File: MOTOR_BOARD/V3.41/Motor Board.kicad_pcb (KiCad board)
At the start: 2 copper layers, 90.9 x 130.4 mm, 173 parts, among them J1 RJ12, K10 CONN_2, K2 CONN_4, K3 CONN_4, K4 CONN_3, K5 CONN_3, K8 COLONETTE, K9 COLONETTE, P1 CAVALIER, P10 CAVALIER, P11 CONN_4, P2 CONN_4, P3 CAVALIER, P4 CONN_6, P5 CONN_4, P6 CONN_5, P7 CONN_4, P8 CONN_4, P9 CAVALIER, Q1 MOS_N, Q10 2N7002, Q11 2N7002, Q2 MOS_N, Q3 MOS_N, Q4 MOS_N, Q5 MOS_N, Q6 MOS_N, Q7 MOS_N, Q8 MOS_N, Q9 2N7002, SW2 SW_PUSH_SMALL, U1 PCA9306, U10 PIC32MX795F512H, U11 74LVCC3245, U12 74LVCC3245, U13 74LVCC3245, U14 PCA9306, U15 PCF8563, U2 HCTL-2032, U3 74HC02, U4 LM5104, U5 LM5104, U6 74HC02, U7 LM5104, U8 LM5104, U9 24C512, X1 CRYSTAL1

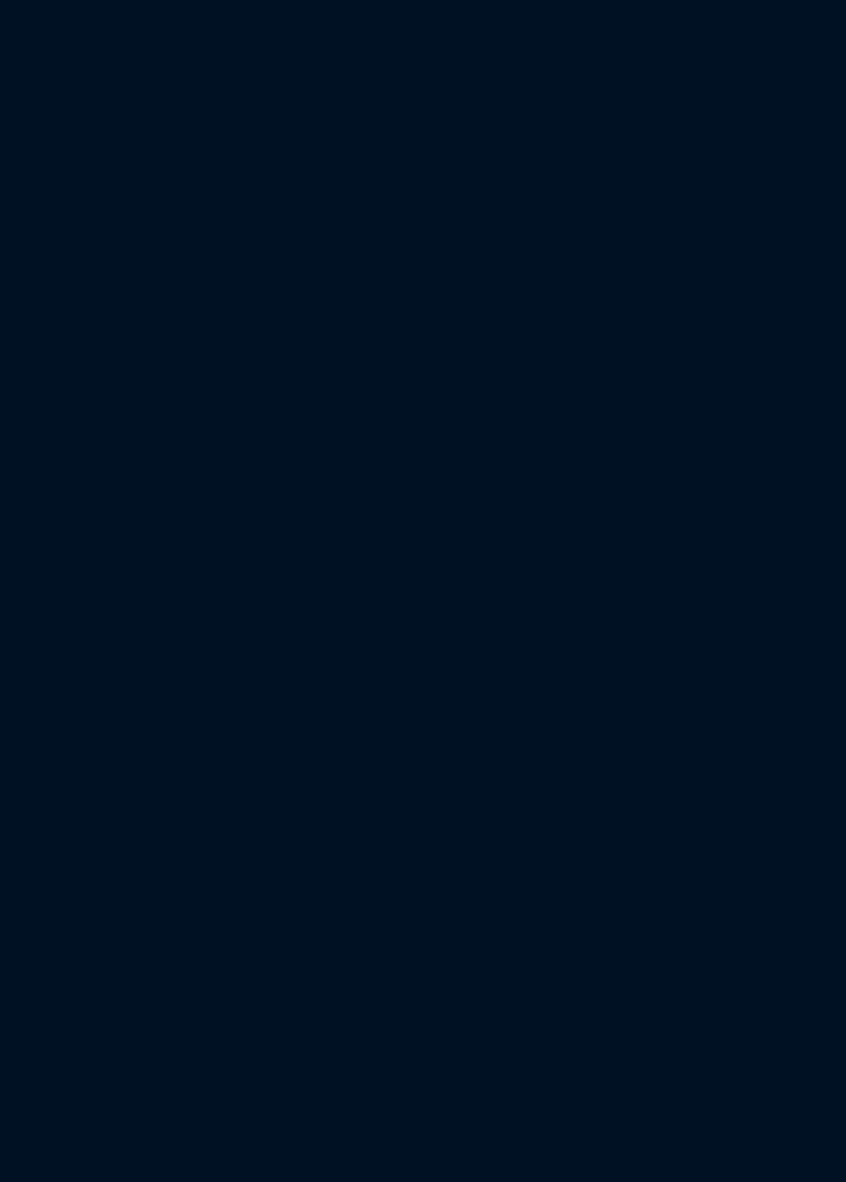
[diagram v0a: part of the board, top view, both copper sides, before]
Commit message: MAJ USB TO 4UART + ADD NEW MECHANICAL BOARD
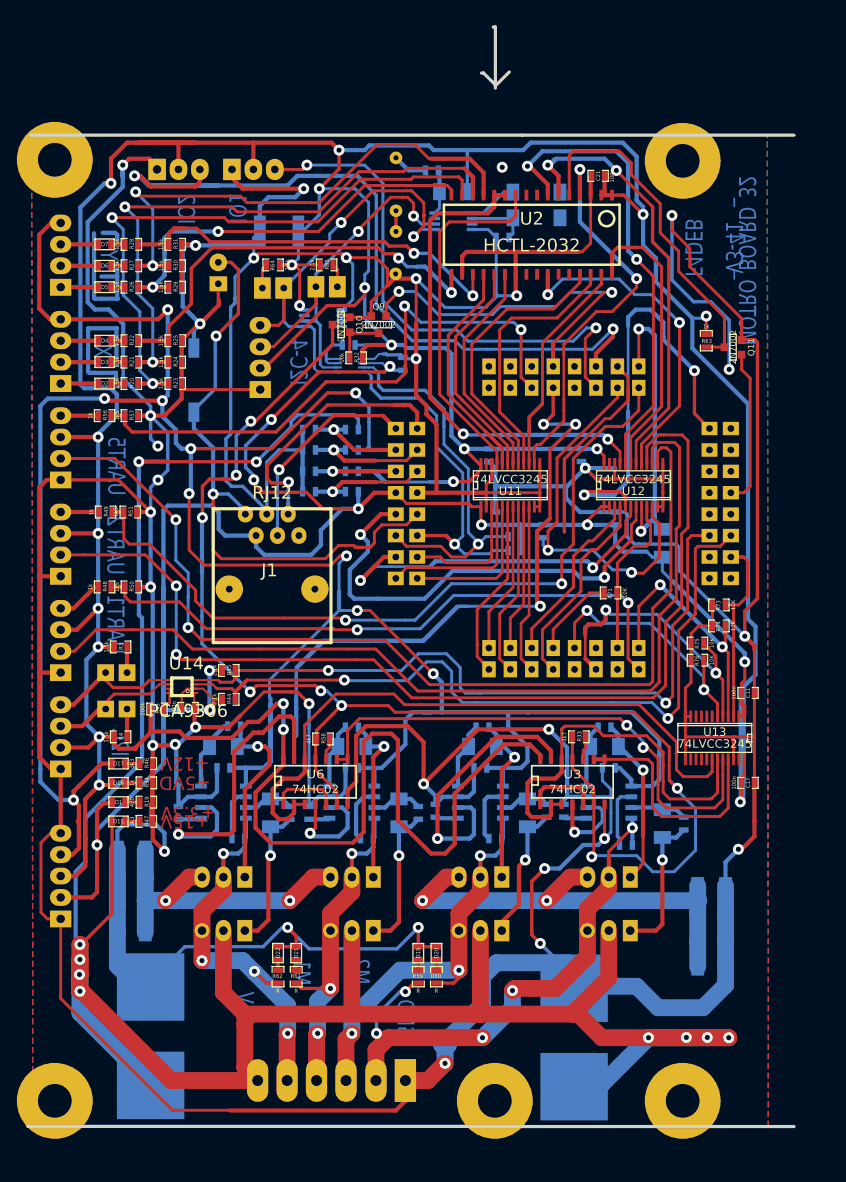
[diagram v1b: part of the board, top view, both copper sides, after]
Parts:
- added 1PIN: P***, 1pin, B.Cu at (50.1, 47.6)
- added C1: 2200u, C_14x16, B.Cu at (61.5, 157.4)
- added C10: 100n, SM0603_Capa, B.Cu at (70.1, 119.8)
- added C11: 100n, SM0603_Capa, F.Cu at (132.3, 110.9)
- added C12: 100n, SM0603_Capa, F.Cu at (65.9, 112.6)
- added C13: 100n, SM0603_Capa, B.Cu at (116.6, 90.2)
- added C14: 100n, SM0603_Capa, B.Cu at (102.4, 90.2)
- added C15: 100n, SM0603_Capa, B.Cu at (101.6, 82.7)
- added C16: 100n, SM0603_Capa, B.Cu at (112.6, 82.7)
- added C17: 100n, SM0603_Capa, F.Cu at (132.3, 121.5)
- added C18: 47u, SM1812, B.Cu at (76.7, 56.1)
- added C19: 2200u, C_14x16, B.Cu at (111.7, 157.6)
- added C2: 100n, SM0603_Capa, B.Cu at (91.4, 71.8)
- added C20: CP, C-10F, B.Cu at (94.4, 44.1)
- added C21: 100n, SM0603_Capa, F.Cu at (114.6, 49.5)
- added C22: CP, C-10F, B.Cu at (94.4, 56.3)
- added C23: C, SM0603_Capa, B.Cu at (103.2, 56.8)
- added C3: 100n, SM0603_Capa, B.Cu at (117.9, 128.9)
- added C4: 100n, SM0603_Capa, B.Cu at (102.4, 128.1)
- added C5: 100n, SM0603_Capa, B.Cu at (115.8, 119.8)
- added C6: 100n, SM0603_Capa, B.Cu at (100.6, 119.8)
- added C7: 100n, SM0603_Capa, B.Cu at (87.1, 128.1)
- added C8: 100n, SM0603_Capa, B.Cu at (71.9, 128.1)
- added C9: 100n, SM0603_Capa, B.Cu at (85.3, 119.8)
- added COLONETTE: VAL**, COLONETTE, B.Cu at (50.1, 47.6)
- added COLONETTE: VAL**, COLONETTE, B.Cu at (102.3, 159.3)
- added COLONETTE: VAL**, COLONETTE, B.Cu at (50.1, 159.3)
- added D1: VERT, SM0603, F.Cu at (57.7, 123.8)
- added D10: DIODE, SM1206, B.Cu at (115.3, 117.2)
- added D11: DIODE, SM1206, B.Cu at (100.8, 117.2)
- added D12: DIODE, SM1206, B.Cu at (90.9, 125.1)
- added D13: DIODE, SM1206, B.Cu at (75.7, 125.1)
- added D14: DIODE, SM1206, B.Cu at (85.3, 117.2)
- added D15: DIODE, SM1206, B.Cu at (70.1, 117.2)
- added D16: VERT, SM0603, F.Cu at (57.7, 121.5)
- added D17: VERT, SM0603, F.Cu at (57.7, 119.3)
- added D18: VERT, SM0603, F.Cu at (57.7, 126.1)
- added D19: LED, SM0603, F.Cu at (93.2, 141.7)
- added D2: JAUNE, SM0603, F.Cu at (56.0, 74.2)
- added D20: LED, SM0603, F.Cu at (95.4, 141.7)
- added D21: LED, SM0603, F.Cu at (78.7, 141.7)
- added D22: LED, SM0603, F.Cu at (76.6, 141.7)
- added D23: DIODESCH, SM1206, B.Cu at (97.4, 51.4)
- added D3: JAUNE, SM0603, F.Cu at (56.0, 71.6)
- added D4: JAUNE, SM0603, F.Cu at (56.0, 69.1)
- added D5: JAUNE, SM0603, F.Cu at (56.0, 62.7)
- added D6: JAUNE, SM0603, F.Cu at (56.0, 60.2)
- added D7: JAUNE, SM0603, F.Cu at (56.0, 57.7)
- added D8: DIODE, SM1206, B.Cu at (122.2, 126.4)
- added D9: DIODE, SM1206, B.Cu at (106.2, 125.1)
- added J1: RJ12, RJ12_E, F.Cu at (75.9, 89.7)
- added K10: CONN_2, KK-2, B.Cu at (69.5, 59.8)
- added K2: CONN_4, KK-4, B.Cu at (50.8, 66.5)
- added K3: CONN_4, KK-4, B.Cu at (50.8, 55.1)
- added K4: CONN_3, KK-3, B.Cu at (67.3, 48.8)
- added K5: CONN_3, KK-3, B.Cu at (76.2, 48.8)
- added K8: COLONETTE, COLONETTE, B.Cu at (124.6, 159.3)
- added K9: COLONETTE, COLONETTE, B.Cu at (124.6, 47.8)
- added P1: CAVALIER, CAVALIER, B.Cu at (56.1, 108.5)
- added P10: CAVALIER, CAVALIER, B.Cu at (81.1, 62.7)
- added P11: CONN_4, KK-4, B.Cu at (74.5, 67.3)
- added P2: CONN_4, KK-4, B.Cu at (50.8, 112.3)
- added P3: CAVALIER, CAVALIER, B.Cu at (56.1, 112.8)
- added P4: CONN_6, WEIDMULLER-6, B.Cu at (91.7, 156.8)
- added P5: CONN_4, KK-4, B.Cu at (50.8, 89.4)
- added P6: CONN_5, KK-5, B.Cu at (50.8, 130.0)
- added P7: CONN_4, KK-4, B.Cu at (50.8, 78.0)
- added P8: CONN_4, KK-4, B.Cu at (50.8, 100.8)
- added P9: CAVALIER, CAVALIER, B.Cu at (77.3, 62.8)
- added Q1: MOS_N, IRFIZ48V, B.Cu at (115.8, 139.1)
- added Q10: 2N7002, SOT23GDS, F.Cu at (84.1, 67.2)
- added Q11: 2N7002, SOT23GDS, F.Cu at (130.6, 69.8)
- added Q2: MOS_N, IRFIZ48V, B.Cu at (100.6, 139.1)
- added Q3: MOS_N, IRFIZ48V, B.Cu at (115.8, 132.7)
- added Q4: MOS_N, IRFIZ48V, B.Cu at (100.6, 132.7)
- added Q5: MOS_N, IRFIZ48V, B.Cu at (85.3, 139.1)
- added Q6: MOS_N, IRFIZ48V, B.Cu at (70.1, 139.1)
- added Q7: MOS_N, IRFIZ48V, B.Cu at (85.3, 132.7)
- added Q8: MOS_N, IRFIZ48V, B.Cu at (70.1, 132.7)
- added Q9: 2N7002, SOT23GDS, F.Cu at (88.5, 67.2)
- added R1: 0.068, SM1206, B.Cu at (128.0, 133.7)
- added R10: 220k, SM0603_Resistor, B.Cu at (95.2, 124.8)
- added R11: 0.068, SM1206, B.Cu at (128.0, 143.4)
- added R12: 47, SM0603_Resistor, B.Cu at (93.2, 125.1)
- added R13: 47, SM0603_Resistor, B.Cu at (78.0, 125.1)
- added R14: 220k, SM0603_Resistor, B.Cu at (80.3, 125.1)
- added R15: 47, SM0603_Resistor, B.Cu at (85.3, 114.9)
- added R16: 47, SM0603_Resistor, B.Cu at (71.4, 114.8)
- added R17: 220k, SM0603_Resistor, B.Cu at (64.8, 125.1)
- added R18: 0.068, SM1206, B.Cu at (59.2, 129.4)
- added R19: 470, SM0603_Resistor, F.Cu at (61.0, 123.8)
- added R2: 0.068, SM1206, B.Cu at (128.0, 140.3)
- added R20: 1.5k, SM0603_Resistor, F.Cu at (59.2, 74.2)
- added R21: 1.5k, SM0603_Resistor, F.Cu at (59.2, 71.6)
- added R22: 1.5k, SM0603_Resistor, F.Cu at (59.2, 69.1)
- added R23: 1.5k, SM0603_Resistor, F.Cu at (64.4, 74.2)
- added R24: 1.5k, SM0603_Resistor, F.Cu at (64.4, 71.6)
- added R25: 1.5k, SM0603_Resistor, F.Cu at (64.4, 69.1)
- added R26: 1.5k, SM0603_Resistor, F.Cu at (59.2, 62.7)
- added R27: 1.5k, SM0603_Resistor, F.Cu at (59.2, 60.2)
- added R28: 1.5k, SM0603_Resistor, F.Cu at (59.2, 57.7)
- added R29: 1.5k, SM0603_Resistor, F.Cu at (64.4, 62.7)
- added R3: 1.5k, SM0603_Resistor, F.Cu at (57.9, 105.4)
- added R30: 1.5k, SM0603_Resistor, F.Cu at (64.4, 60.2)
- added R31: 1.5k, SM0603_Resistor, F.Cu at (64.4, 57.7)
- added R32: 10k, SM0603_Resistor, F.Cu at (85.9, 71.1)
- added R33: 4k7, SM0603_Resistor, F.Cu at (112.3, 116.1)
- added R34: 1k, SM0603_Resistor, F.Cu at (61.0, 121.5)
- added R35: 10k 1%, SM0603_Resistor, B.Cu at (85.3, 79.6)
- added R36: 10k 1%, SM0603_Resistor, B.Cu at (85.3, 82.0)
- added R37: 10k 1%, SM0603_Resistor, B.Cu at (85.3, 84.6)
- added R38: 10k 1%, SM0603_Resistor, B.Cu at (85.3, 87.0)
- added R39: 1k 1%, SM0603_Resistor, B.Cu at (80.3, 79.6)
- added R4: 1.5k, SM0603_Resistor, F.Cu at (57.9, 116.1)
- added R40: 1k 1%, SM0603_Resistor, B.Cu at (80.3, 82.0)
- added R41: 1k 1%, SM0603_Resistor, B.Cu at (80.3, 84.6)
- added R42: 1k 1%, SM0603_Resistor, B.Cu at (80.3, 87.0)
- added R43: 200k, SM0603_Resistor, F.Cu at (62.2, 112.8)
- added R44: 2.1k, SM0603_Resistor, F.Cu at (70.7, 111.6)
- added R45: 2.1k, SM0603_Resistor, F.Cu at (70.7, 108.2)
- added R46: 3k3, SM0603_Resistor, F.Cu at (61.0, 119.3)
- added R47: 3k3, SM0603_Resistor, F.Cu at (61.0, 126.1)
- added R48: 1k, SM0603_Resistor, F.Cu at (56.0, 98.3)
- added R49: 1k, SM0603_Resistor, F.Cu at (56.1, 89.4)
- added R5: 47, SM0603_Resistor, B.Cu at (124.7, 126.4)
- added R50: 1k5, SM0603_Resistor, F.Cu at (59.2, 98.3)
- added R51: 1k5, SM0603_Resistor, F.Cu at (59.1, 89.4)
- added R52: 0.068, SM1206, B.Cu at (128.0, 137.0)
- added R53: 0.068, SM1206, B.Cu at (59.2, 136.0)
- added R54: 0.068, SM1206, B.Cu at (59.2, 139.3)
- added R55: 0.068, SM1206, B.Cu at (59.2, 132.7)
- added R56: 1k, SM0603_Resistor, F.Cu at (56.0, 78.0)
- added R57: 1k5, SM0603_Resistor, F.Cu at (59.2, 78.0)
- added R58: 4k7, SM0603_Resistor, F.Cu at (81.9, 116.3)
- added R59: R, SM0603_Resistor, F.Cu at (93.2, 144.5)
- added R6: 47, SM0603_Resistor, B.Cu at (108.5, 124.8)
- added R60: R, SM0603_Resistor, F.Cu at (95.4, 144.5)
- added R61: R, SM0603_Resistor, F.Cu at (78.7, 144.5)
- added R62: R, SM0603_Resistor, F.Cu at (76.6, 144.5)
- added R63: 1k, SM0603_Resistor, F.Cu at (127.4, 69.1)
- added R64: 2.1k, SM0603_Resistor, F.Cu at (76.0, 60.1)
- added R65: 2.1k, SM0603_Resistor, F.Cu at (82.3, 60.1)
- added R66: 2.1k, SM0603_Resistor, B.Cu at (104.6, 92.3)
- added R67: 2.1k, SM0603_Resistor, B.Cu at (104.6, 94.0)
- added R68: 200k, SM0603_Resistor, B.Cu at (85.0, 69.6)
- added R69: 150, SM0603_Resistor, B.Cu at (94.8, 48.9)
- added R7: 220k, SM0603_Resistor, B.Cu at (110.5, 124.8)
- added R70: 10K, SM1206, B.Cu at (122.2, 93.1)
- added R71: 10K, SM0603_Resistor, F.Cu at (116.0, 99.0)
- added R72: 10K, SM0603_Resistor, B.Cu at (108.1, 91.7)
- added R73: 10K, SM0603_Resistor, F.Cu at (128.9, 100.4)
- added R74: 10K, SM0603_Resistor, F.Cu at (128.9, 102.9)
- added R75: 10K, SM0603_Resistor, F.Cu at (126.3, 105.0)
- added R76: 10K, SM0603_Resistor, F.Cu at (126.3, 107.0)
- added R8: 47, SM0603_Resistor, B.Cu at (115.3, 114.9)
- added R9: 47, SM0603_Resistor, B.Cu at (100.8, 114.9)
- added SW2: SW_PUSH_SMALL, SW2, B.Cu at (66.6, 77.6)
- added U1: PCA9306, VSSOP-8, B.Cu at (85.1, 72.0)
- added U10: PIC32MX795F512H, PIC32½64, B.Cu at (90.6, 97.3)
- added U11: 74LVCC3245, SSOP24, F.Cu at (104.1, 86.2)
- added U12: 74LVCC3245, SSOP24, F.Cu at (118.7, 86.2)
- added U13: 74LVCC3245, SSOP24, F.Cu at (128.4, 116.2)
- added U14: PCA9306, VSSOP-8, F.Cu at (65.2, 110.1)
- added U15: PCF8563, SSOP8, B.Cu at (97.4, 54.9)
- added U2: HCTL-2032, SOJ32, F.Cu at (106.7, 56.5)
- added U3: 74HC02, SO14E, F.Cu at (111.5, 121.3)
- added U4: LM5104, SO8E, B.Cu at (115.8, 123.8)
- added U5: LM5104, SO8E, B.Cu at (100.6, 123.8)
- added U6: 74HC02, SO14E, F.Cu at (81.0, 121.3)
- added U7: LM5104, SO8E, B.Cu at (85.3, 123.8)
- added U8: LM5104, SO8E, B.Cu at (70.1, 123.8)
- added U9: 24C512, SSOP8, B.Cu at (81.9, 66.4)
- added X1: CRYSTAL1, LFXTAL003000, B.Cu at (104.4, 51.5)
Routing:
- net GND: track 1129.3 -> 2258.6 mm, vias 32 -> 64
- net +5VD: track 608.7 -> 1217.4 mm, vias 21 -> 42
- net +12V: track 329.9 -> 659.7 mm, vias 10 -> 20
- net +15V: track 299.9 -> 599.8 mm, vias 10 -> 20
- net +3.3V: track 290.3 -> 580.6 mm, vias 10 -> 20
- net (no net): track 185.1 -> 370.2 mm, vias 4 -> 8
- net N-00000193: track 167.5 -> 335.0 mm, vias 8 -> 16
- net /PIC30F4013/U2TX: track 122.1 -> 244.2 mm, vias 2 -> 4
- net /PIC30F4013/U5TX: track 119.7 -> 239.5 mm, vias 2 -> 4
- net /PIC30F4013/U1TX: track 110.0 -> 220.0 mm
- net /PIC30F4013/IO2: track 102.2 -> 204.5 mm, vias 2 -> 4
- net /PIC30F4013/RX2: track 91.6 -> 183.2 mm, vias 2 -> 4
- net N-0000062: track 91.5 -> 183.0 mm, vias 2 -> 4
- net N-0000061: track 85.2 -> 170.5 mm, vias 2 -> 4
- net /MOTOR/DIR2: track 76.1 -> 152.2 mm
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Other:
- board size 90.9 x 130.4 mm -> 212.2 x 131.4 mm
